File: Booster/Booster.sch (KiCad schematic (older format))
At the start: 14 parts

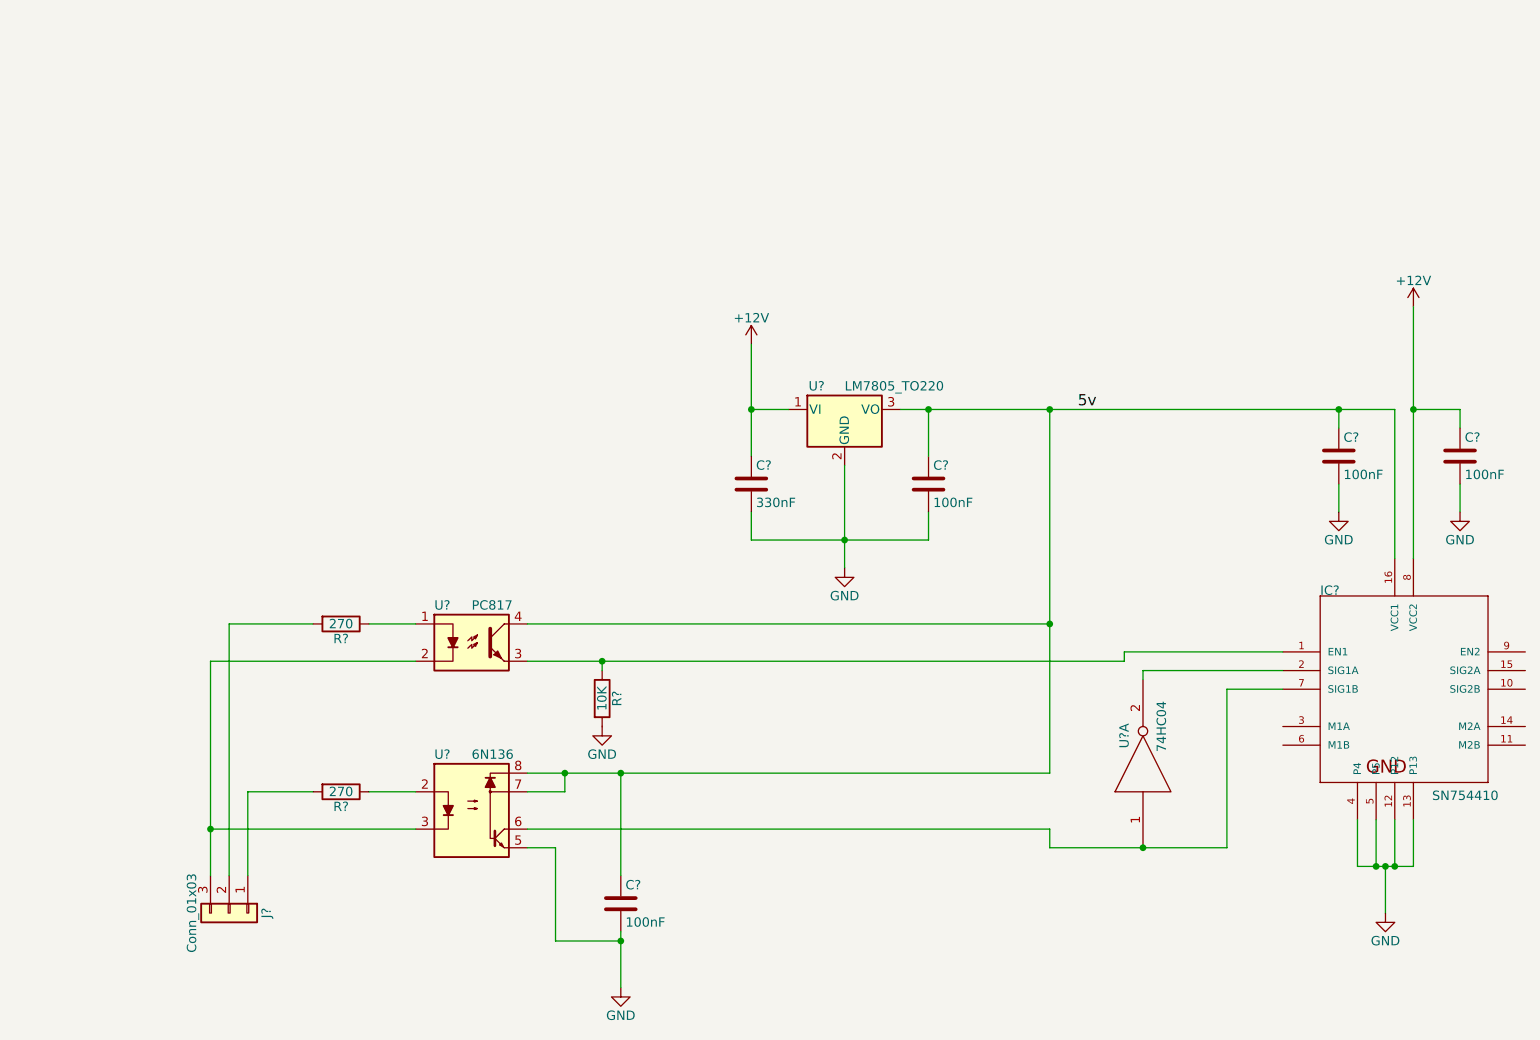
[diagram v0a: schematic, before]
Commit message: Fixed missing pull-up on 6n137 optocoupler driving the DCC signal. Moved power, DCC input and track output to separate sheets.
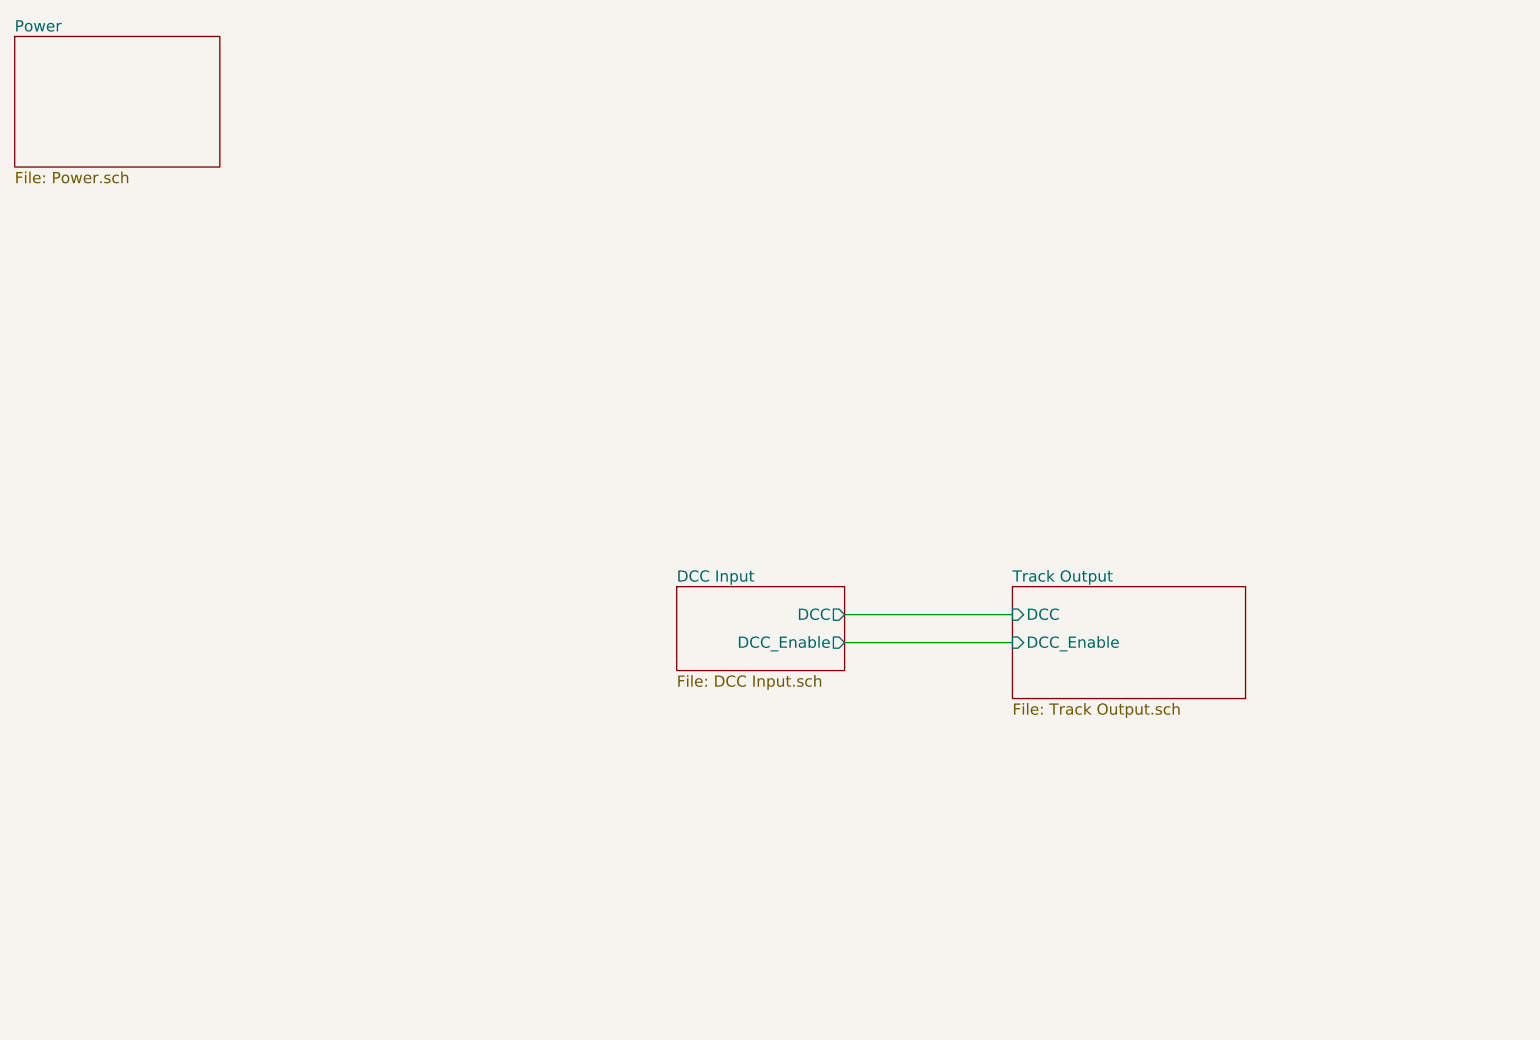
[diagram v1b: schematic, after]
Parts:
- removed C? (x4): 100nF, symbol C
- removed C?: 330nF, symbol C
- removed IC?: SN754410, HBridge-DIP16, symbol SN754410
- removed J?: Conn_01x03, symbol Conn_01x03
- removed R? (x2): 270, symbol R
- removed R?: 10K, symbol R
- removed U?: LM7805_TO220, TO_SOT_Packages_THT:TO-220_Vertical, symbol LM7805_TO220
- removed U?: 6N136, Housings_DIP:DIP-8_W7.62mm, symbol 6N136
- removed U?: PC817, Housings_DIP:DIP-4_W7.62mm, symbol PC817
- removed U?: 74HC04, symbol 74HC04
